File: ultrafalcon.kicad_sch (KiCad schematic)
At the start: 43 parts, among them J1 Conn_01x08_Socket, SW1 RotaryEncoder, SW2 SW_Push, U1 SK6805-EC15, U10 SK6805-EC15, U11 SK6805-EC15, U12 SK6805-EC15, U13 SK6805-EC15, U14 SK6805-EC15, U15 SK6805-EC15, U16 SK6805-EC15, U17 SK6805-EC15, U18 SK6805-EC15, U19 SK6805-EC15, U2 SK6805-EC15, U20 SK6805-EC15, U21 SK6805-EC15, U22 SK6805-EC15, U23 SK6805-EC15, U24 SK6805-EC15, U25 SK6805-EC15, U26 SK6805-EC15, U27 SK6805-EC15, U28 SK6805-EC15, U29 SK6805-EC15, U3 SK6805-EC15, U30 SK6805-EC15, U4 SK6805-EC15, U5 SK6805-EC15, U6 SK6805-EC15, U7 SK6805-EC15, U8 SK6805-EC15, U9 SK6805-EC15

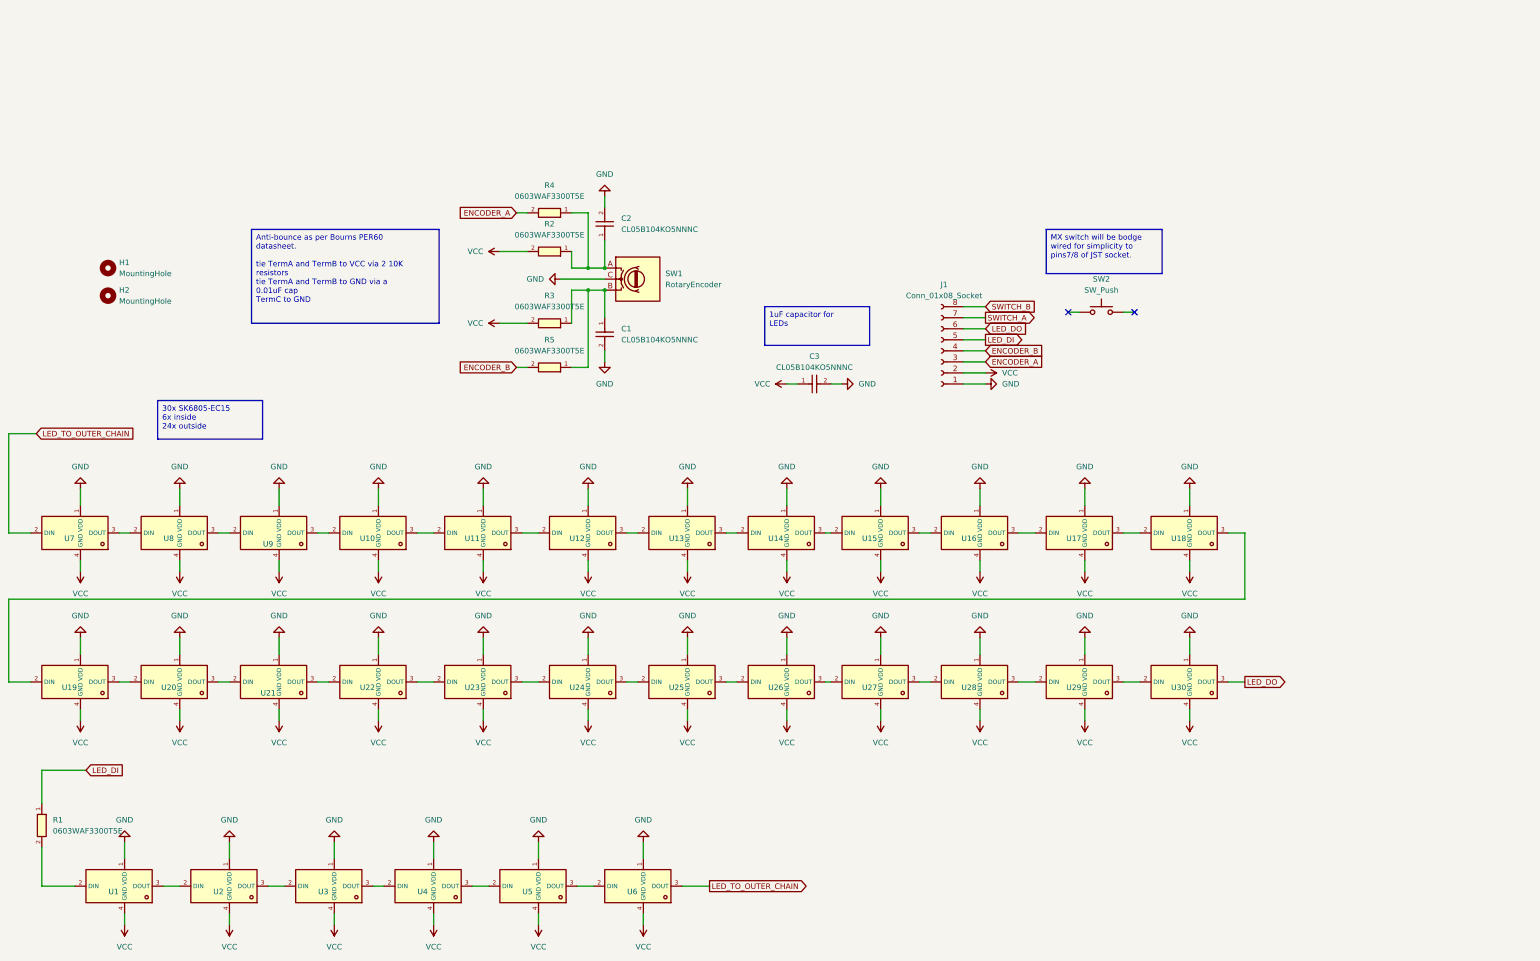
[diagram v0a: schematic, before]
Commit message: replacing the led footprint and symbol, doing the tracing
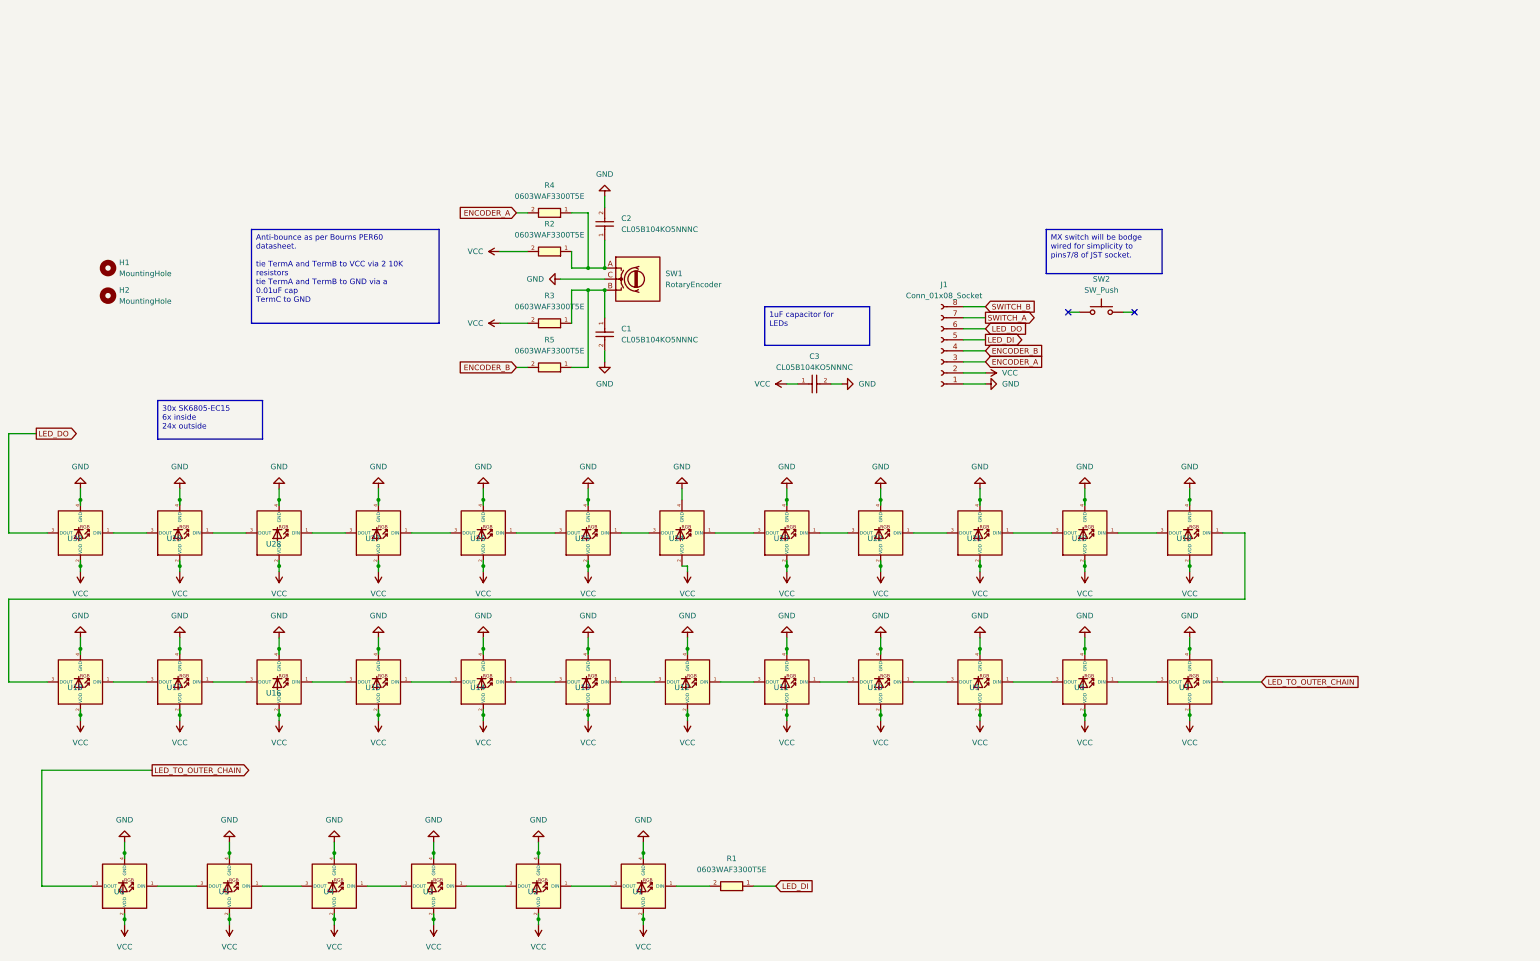
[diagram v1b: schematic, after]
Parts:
- U1: renamed from U6; footprint ct-kicad:LED-SMD_4P-L1.5-W1.5-BL -> ct-kicad:LED_dilemma_SK6805-EC15_1.5x1.5mm_P0.6mm_handsolder; MFN (none) -> Dongguan Opsco Optoelectronics; MPN (none) -> SK6805-EC15; PKG (none) -> SK6805-EC15
- U10: renamed from U27; footprint ct-kicad:LED-SMD_4P-L1.5-W1.5-BL -> ct-kicad:LED_dilemma_SK6805-EC15_1.5x1.5mm_P0.6mm_handsolder; MFN (none) -> Dongguan Opsco Optoelectronics; MPN (none) -> SK6805-EC15; PKG (none) -> SK6805-EC15
- U11: renamed from U26; footprint ct-kicad:LED-SMD_4P-L1.5-W1.5-BL -> ct-kicad:LED_dilemma_SK6805-EC15_1.5x1.5mm_P0.6mm_handsolder; MFN (none) -> Dongguan Opsco Optoelectronics; MPN (none) -> SK6805-EC15; PKG (none) -> SK6805-EC15
- U12: renamed from U25; footprint ct-kicad:LED-SMD_4P-L1.5-W1.5-BL -> ct-kicad:LED_dilemma_SK6805-EC15_1.5x1.5mm_P0.6mm_handsolder; MFN (none) -> Dongguan Opsco Optoelectronics; MPN (none) -> SK6805-EC15; PKG (none) -> SK6805-EC15
- U13: renamed from U24; footprint ct-kicad:LED-SMD_4P-L1.5-W1.5-BL -> ct-kicad:LED_dilemma_SK6805-EC15_1.5x1.5mm_P0.6mm_handsolder; MFN (none) -> Dongguan Opsco Optoelectronics; MPN (none) -> SK6805-EC15; PKG (none) -> SK6805-EC15
- U14: renamed from U23; footprint ct-kicad:LED-SMD_4P-L1.5-W1.5-BL -> ct-kicad:LED_dilemma_SK6805-EC15_1.5x1.5mm_P0.6mm_handsolder; MFN (none) -> Dongguan Opsco Optoelectronics; MPN (none) -> SK6805-EC15; PKG (none) -> SK6805-EC15
- U15: renamed from U22; footprint ct-kicad:LED-SMD_4P-L1.5-W1.5-BL -> ct-kicad:LED_dilemma_SK6805-EC15_1.5x1.5mm_P0.6mm_handsolder; MFN (none) -> Dongguan Opsco Optoelectronics; MPN (none) -> SK6805-EC15; PKG (none) -> SK6805-EC15
- U16: renamed from U21; footprint ct-kicad:LED-SMD_4P-L1.5-W1.5-BL -> ct-kicad:LED_dilemma_SK6805-EC15_1.5x1.5mm_P0.6mm_handsolder; MFN (none) -> Dongguan Opsco Optoelectronics; MPN (none) -> SK6805-EC15; PKG (none) -> SK6805-EC15
- U17: renamed from U20; footprint ct-kicad:LED-SMD_4P-L1.5-W1.5-BL -> ct-kicad:LED_dilemma_SK6805-EC15_1.5x1.5mm_P0.6mm_handsolder; MFN (none) -> Dongguan Opsco Optoelectronics; MPN (none) -> SK6805-EC15; PKG (none) -> SK6805-EC15
- U18: renamed from U19; footprint ct-kicad:LED-SMD_4P-L1.5-W1.5-BL -> ct-kicad:LED_dilemma_SK6805-EC15_1.5x1.5mm_P0.6mm_handsolder; MFN (none) -> Dongguan Opsco Optoelectronics; MPN (none) -> SK6805-EC15; PKG (none) -> SK6805-EC15
- U19: renamed from U18; footprint ct-kicad:LED-SMD_4P-L1.5-W1.5-BL -> ct-kicad:LED_dilemma_SK6805-EC15_1.5x1.5mm_P0.6mm_handsolder; MFN (none) -> Dongguan Opsco Optoelectronics; MPN (none) -> SK6805-EC15; PKG (none) -> SK6805-EC15
- U2: renamed from U5; footprint ct-kicad:LED-SMD_4P-L1.5-W1.5-BL -> ct-kicad:LED_dilemma_SK6805-EC15_1.5x1.5mm_P0.6mm_handsolder; MFN (none) -> Dongguan Opsco Optoelectronics; MPN (none) -> SK6805-EC15; PKG (none) -> SK6805-EC15
- U20: renamed from U17; footprint ct-kicad:LED-SMD_4P-L1.5-W1.5-BL -> ct-kicad:LED_dilemma_SK6805-EC15_1.5x1.5mm_P0.6mm_handsolder; MFN (none) -> Dongguan Opsco Optoelectronics; MPN (none) -> SK6805-EC15; PKG (none) -> SK6805-EC15
- U21: renamed from U16; footprint ct-kicad:LED-SMD_4P-L1.5-W1.5-BL -> ct-kicad:LED_dilemma_SK6805-EC15_1.5x1.5mm_P0.6mm_handsolder; MFN (none) -> Dongguan Opsco Optoelectronics; MPN (none) -> SK6805-EC15; PKG (none) -> SK6805-EC15
- U22: renamed from U15; footprint ct-kicad:LED-SMD_4P-L1.5-W1.5-BL -> ct-kicad:LED_dilemma_SK6805-EC15_1.5x1.5mm_P0.6mm_handsolder; MFN (none) -> Dongguan Opsco Optoelectronics; MPN (none) -> SK6805-EC15; PKG (none) -> SK6805-EC15
- U23: renamed from U14; footprint ct-kicad:LED-SMD_4P-L1.5-W1.5-BL -> ct-kicad:LED_dilemma_SK6805-EC15_1.5x1.5mm_P0.6mm_handsolder; MFN (none) -> Dongguan Opsco Optoelectronics; MPN (none) -> SK6805-EC15; PKG (none) -> SK6805-EC15
- U24: renamed from U13; footprint ct-kicad:LED-SMD_4P-L1.5-W1.5-BL -> ct-kicad:LED_dilemma_SK6805-EC15_1.5x1.5mm_P0.6mm_handsolder; MFN (none) -> Dongguan Opsco Optoelectronics; MPN (none) -> SK6805-EC15; PKG (none) -> SK6805-EC15
- U25: renamed from U12; footprint ct-kicad:LED-SMD_4P-L1.5-W1.5-BL -> ct-kicad:LED_dilemma_SK6805-EC15_1.5x1.5mm_P0.6mm_handsolder; MFN (none) -> Dongguan Opsco Optoelectronics; MPN (none) -> SK6805-EC15; PKG (none) -> SK6805-EC15
- U26: renamed from U11; footprint ct-kicad:LED-SMD_4P-L1.5-W1.5-BL -> ct-kicad:LED_dilemma_SK6805-EC15_1.5x1.5mm_P0.6mm_handsolder; MFN (none) -> Dongguan Opsco Optoelectronics; MPN (none) -> SK6805-EC15; PKG (none) -> SK6805-EC15
- U27: renamed from U10; footprint ct-kicad:LED-SMD_4P-L1.5-W1.5-BL -> ct-kicad:LED_dilemma_SK6805-EC15_1.5x1.5mm_P0.6mm_handsolder; MFN (none) -> Dongguan Opsco Optoelectronics; MPN (none) -> SK6805-EC15; PKG (none) -> SK6805-EC15
- U28: renamed from U9; footprint ct-kicad:LED-SMD_4P-L1.5-W1.5-BL -> ct-kicad:LED_dilemma_SK6805-EC15_1.5x1.5mm_P0.6mm_handsolder; MFN (none) -> Dongguan Opsco Optoelectronics; MPN (none) -> SK6805-EC15; PKG (none) -> SK6805-EC15
- U29: renamed from U8; footprint ct-kicad:LED-SMD_4P-L1.5-W1.5-BL -> ct-kicad:LED_dilemma_SK6805-EC15_1.5x1.5mm_P0.6mm_handsolder; MFN (none) -> Dongguan Opsco Optoelectronics; MPN (none) -> SK6805-EC15; PKG (none) -> SK6805-EC15
- U3: renamed from U4; footprint ct-kicad:LED-SMD_4P-L1.5-W1.5-BL -> ct-kicad:LED_dilemma_SK6805-EC15_1.5x1.5mm_P0.6mm_handsolder; MFN (none) -> Dongguan Opsco Optoelectronics; MPN (none) -> SK6805-EC15; PKG (none) -> SK6805-EC15
- U30: renamed from U7; footprint ct-kicad:LED-SMD_4P-L1.5-W1.5-BL -> ct-kicad:LED_dilemma_SK6805-EC15_1.5x1.5mm_P0.6mm_handsolder; MFN (none) -> Dongguan Opsco Optoelectronics; MPN (none) -> SK6805-EC15; PKG (none) -> SK6805-EC15
- U4: renamed from U3; footprint ct-kicad:LED-SMD_4P-L1.5-W1.5-BL -> ct-kicad:LED_dilemma_SK6805-EC15_1.5x1.5mm_P0.6mm_handsolder; MFN (none) -> Dongguan Opsco Optoelectronics; MPN (none) -> SK6805-EC15; PKG (none) -> SK6805-EC15
- U5: renamed from U2; footprint ct-kicad:LED-SMD_4P-L1.5-W1.5-BL -> ct-kicad:LED_dilemma_SK6805-EC15_1.5x1.5mm_P0.6mm_handsolder; MFN (none) -> Dongguan Opsco Optoelectronics; MPN (none) -> SK6805-EC15; PKG (none) -> SK6805-EC15
- U6: renamed from U1; footprint ct-kicad:LED-SMD_4P-L1.5-W1.5-BL -> ct-kicad:LED_dilemma_SK6805-EC15_1.5x1.5mm_P0.6mm_handsolder; MFN (none) -> Dongguan Opsco Optoelectronics; MPN (none) -> SK6805-EC15; PKG (none) -> SK6805-EC15
- U7: renamed from U30; footprint ct-kicad:LED-SMD_4P-L1.5-W1.5-BL -> ct-kicad:LED_dilemma_SK6805-EC15_1.5x1.5mm_P0.6mm_handsolder; MFN (none) -> Dongguan Opsco Optoelectronics; MPN (none) -> SK6805-EC15; PKG (none) -> SK6805-EC15
- U8: renamed from U29; footprint ct-kicad:LED-SMD_4P-L1.5-W1.5-BL -> ct-kicad:LED_dilemma_SK6805-EC15_1.5x1.5mm_P0.6mm_handsolder; MFN (none) -> Dongguan Opsco Optoelectronics; MPN (none) -> SK6805-EC15; PKG (none) -> SK6805-EC15
- U9: renamed from U28; footprint ct-kicad:LED-SMD_4P-L1.5-W1.5-BL -> ct-kicad:LED_dilemma_SK6805-EC15_1.5x1.5mm_P0.6mm_handsolder; MFN (none) -> Dongguan Opsco Optoelectronics; MPN (none) -> SK6805-EC15; PKG (none) -> SK6805-EC15
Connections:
- net GND: now also U1.4 (GND), U10.4 (GND), U11.4 (GND), U12.4 (GND), U13.4 (GND), U14.4 (GND), U15.4 (GND), U16.4 (GND), U17.4 (GND), U18.4 (GND), U19.4 (GND), U2.4 (GND), U20.4 (GND), U21.4 (GND), U22.4 (GND), U23.4 (GND), U24.4 (GND), U25.4 (GND), U26.4 (GND), U27.4 (GND), U28.4 (GND), U29.4 (GND), U3.4 (GND), U30.4 (GND), U4.4 (GND), U5.4 (GND), U6.4 (GND), U7.4 (GND), U8.4 (GND), U9.4 (GND); no longer U1.1 (VDD), U10.1 (VDD), U11.1 (VDD), U12.1 (VDD), U13.1 (VDD), U14.1 (VDD), U15.1 (VDD), U16.1 (VDD), U17.1 (VDD), U18.1 (VDD), U19.1 (VDD), U2.1 (VDD), U20.1 (VDD), U21.1 (VDD), U22.1 (VDD), U23.1 (VDD), U24.1 (VDD), U25.1 (VDD), U26.1 (VDD), U27.1 (VDD), U28.1 (VDD), U29.1 (VDD), U3.1 (VDD), U30.1 (VDD), U4.1 (VDD), U5.1 (VDD), U6.1 (VDD), U7.1 (VDD), U8.1 (VDD), U9.1 (VDD)
- net LED_DO: now also U30.3 (DOUT); no longer U7.3 (DOUT)
- net LED_TO_OUTER_CHAIN: now also U6.3 (DOUT), U7.1 (DIN); no longer U1.3 (DOUT), U30.2 (DIN)
- net VCC: now also U1.2 (VDD), U10.2 (VDD), U11.2 (VDD), U12.2 (VDD), U13.2 (VDD), U14.2 (VDD), U15.2 (VDD), U16.2 (VDD), U17.2 (VDD), U18.2 (VDD), U19.2 (VDD), U2.2 (VDD), U20.2 (VDD), U21.2 (VDD), U22.2 (VDD), U23.2 (VDD), U24.2 (VDD), U25.2 (VDD), U26.2 (VDD), U27.2 (VDD), U28.2 (VDD), U29.2 (VDD), U3.2 (VDD), U30.2 (VDD), U4.2 (VDD), U5.2 (VDD), U6.2 (VDD), U7.2 (VDD), U8.2 (VDD), U9.2 (VDD); no longer U1.4 (GND), U10.4 (GND), U11.4 (GND), U12.4 (GND), U13.4 (GND), U14.4 (GND), U15.4 (GND), U16.4 (GND), U17.4 (GND), U18.4 (GND), U19.4 (GND), U2.4 (GND), U20.4 (GND), U21.4 (GND), U22.4 (GND), U23.4 (GND), U24.4 (GND), U25.4 (GND), U26.4 (GND), U27.4 (GND), U28.4 (GND), U29.4 (GND), U3.4 (GND), U30.4 (GND), U4.4 (GND), U5.4 (GND), U6.4 (GND), U7.4 (GND), U8.4 (GND), U9.4 (GND)
- net at U20.3 (DOUT): now also U21.1 (DIN); no longer U19.2 (DIN)
- net at U19.3 (DOUT): now also U20.1 (DIN); no longer U18.2 (DIN)
- net at U27.3 (DOUT): now also U28.1 (DIN); no longer U26.2 (DIN)
- net at U26.3 (DOUT): now also U27.1 (DIN); no longer U25.2 (DIN)
- net at U5.3 (DOUT): now also U6.1 (DIN); no longer U4.2 (DIN)
- net at U4.3 (DOUT): now also U5.1 (DIN); no longer U3.2 (DIN)
- net at R1.2: now also U1.1 (DIN); no longer U6.2 (DIN)
- net at U11.3 (DOUT): now also U12.1 (DIN); no longer U10.2 (DIN)
- net at U10.3 (DOUT): now also U11.1 (DIN); no longer U9.2 (DIN)
- net at U22.3 (DOUT): now also U23.1 (DIN); no longer U21.2 (DIN)
- net at U21.3 (DOUT): now also U22.1 (DIN); no longer U20.2 (DIN)
- net at U12.3 (DOUT): now also U13.1 (DIN); no longer U11.2 (DIN)
- net at U3.3 (DOUT): now also U4.1 (DIN); no longer U2.2 (DIN)
- net at U2.3 (DOUT): now also U3.1 (DIN); no longer U1.2 (DIN)
- net at U23.3 (DOUT): now also U24.1 (DIN); no longer U22.2 (DIN)
- net at U29.3 (DOUT): now also U30.1 (DIN); no longer U28.2 (DIN)
- net at U28.3 (DOUT): now also U29.1 (DIN); no longer U27.2 (DIN)
- net at U14.3 (DOUT): now also U15.1 (DIN); no longer U13.2 (DIN)
- net at U13.3 (DOUT): now also U14.1 (DIN); no longer U12.2 (DIN)
- net at U18.3 (DOUT): now also U19.1 (DIN); no longer U17.2 (DIN)
- net at U25.3 (DOUT): now also U26.1 (DIN); no longer U24.2 (DIN)
- net at U8.3 (DOUT): now also U9.1 (DIN); no longer U7.2 (DIN)
- net at U15.3 (DOUT): now also U16.1 (DIN); no longer U14.2 (DIN)
- net at U16.3 (DOUT): now also U17.1 (DIN); no longer U15.2 (DIN)
- net at U24.3 (DOUT): now also U25.1 (DIN); no longer U23.2 (DIN)
- net at U9.3 (DOUT): now also U10.1 (DIN); no longer U8.2 (DIN)
- net at U17.3 (DOUT): now also U18.1 (DIN); no longer U16.2 (DIN)
- new net: U1.3 (DOUT), U2.1 (DIN)
- new net: U7.3 (DOUT), U8.1 (DIN)

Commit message: moving text around, adding rear labels, updating footprints
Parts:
- added LOGO1: **REF, ct-kicad:awesome-logo, symbol ct-kicad:awesome-logo
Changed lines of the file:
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@@
+    )
+  )
+  (symbol (lib_id "ct-kicad:awesome-logo") (at 41.91 96.52 0) (unit 1)
+    (in_bom no) (on_board yes) (dnp no) (fields_autoplaced)
+    (property "Reference" "LOGO1" (at 44.45 95.25 0)
+      (effects (font (size 1.27 1.27)) (justify left))
+    )
+    (property "Value" "**REF" (at 44.45 97.79 0)
+      (effects (font (size 1.27 1.27)) (justify left))
+    )
+    (property "Footprint" "ct-kicad:awesome-logo" (at 41.91 96.52 0)
+      (effects (font (size 1.27 1.27)) hide)
+    )
+    (property "Datasheet" "" (at 41.91 96.52 0)
+      (effects (font (size 1.27 1.27)) hide)
+    )
+    (instances
+      (project "ultrafalcon"
+        (path "/7e990e0f-d17d-4d94-84c9-ab822ccf2d6e"
+          (reference "LOGO1") (unit 1)
+        )
+      )
     )
   )

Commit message: getting the board ready for pcbway
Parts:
- C1, C2: value CL05B104KO5NNNC -> 0.01uF
- C3: value CL05B104KO5NNNC -> 100uF
- H1, H2, J1, SW2: now left out of the parts list
- R1: value 0603WAF3300T5E -> 330
- R2, R3, R4, R5: value 0603WAF3300T5E -> 10k
- SW1: value RotaryEncoder -> PER601-P117-N0015
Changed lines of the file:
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@@
       (effects (font (size 1.27 1.27)) (justify left))
     )
-    (property "Value" "RotaryEncoder" (at 170.18 86.36 0)
+    (property "Value" "PER601-P117-N0015" (at 170.18 86.36 0)
       (effects (font (size 1.27 1.27)) (justify left))
     )
@@
   )
   (symbol (lib_id "Mechanical:MountingHole") (at 41.91 88.9 0) (unit 1)
-    (in_bom yes) (on_board yes) (dnp no) (fields_autoplaced)
+    (in_bom no) (on_board yes) (dnp no) (fields_autoplaced)
     (property "Reference" "H2" (at 44.45 87.63 0)
       (effects (font (size 1.27 1.27)) (justify left))
@@
       (effects (font (size 1.27 1.27)))
     )
-    (property "Value" "0603WAF3300T5E" (at 143.51 74.93 0)
+    (property "Value" "10k" (at 143.51 74.93 0)
       (effects (font (size 1.27 1.27)))
     )
@@
   )
   (symbol (lib_id "Switch:SW_Push") (at 270.51 92.71 0) (unit 1)
-    (in_bom yes) (on_board yes) (dnp no) (fields_autoplaced)
+    (in_bom no) (on_board yes) (dnp no) (fields_autoplaced)
     (property "Reference" "SW2" (at 270.51 85.09 0)
       (effects (font (size 1.27 1.27)))
@@
       (effects (font (size 1.27 1.27)))
     )
-    (property "Value" "0603WAF3300T5E" (at 143.51 91.44 0)
+    (property "Value" "10k" (at 143.51 91.44 0)
       (effects (font (size 1.27 1.27)))
     )
@@
       (effects (font (size 1.27 1.27)))
     )
-    (property "Value" "CL05B104KO5NNNC" (at 204.47 105.41 0)
+    (property "Value" "100uF" (at 204.47 105.41 0)
       (effects (font (size 1.27 1.27)))
     )
@@
       (effects (font (size 1.27 1.27)))
     )
-    (property "Value" "0603WAF3300T5E" (at 185.42 220.98 0)
+    (property "Value" "330" (at 185.42 220.98 0)
       (effects (font (size 1.27 1.27)))
     )
@@
       (effects (font (size 1.27 1.27)) (justify left))
     )
-    (property "Value" "CL05B104KO5NNNC" (at 160.02 99.06 90)
+    (property "Value" "0.01uF" (at 160.02 99.06 90)
       (effects (font (size 1.27 1.27)) (justify left))
     )
@@
       (effects (font (size 1.27 1.27)) (justify right))
     )
-    (property "Value" "CL05B104KO5NNNC" (at 160.02 73.66 90)
+    (property "Value" "0.01uF" (at 160.02 73.66 90)
       (effects (font (size 1.27 1.27)) (justify right))
     )
@@
       (effects (font (size 1.27 1.27)))
     )
-    (property "Value" "0603WAF3300T5E" (at 143.51 101.6 0)
+    (property "Value" "10k" (at 143.51 101.6 0)
       (effects (font (size 1.27 1.27)))
     )
@@
   )
   (symbol (lib_id "Connector:Conn_01x08_Socket") (at 233.68 101.6 180) (unit 1)
-    (in_bom yes) (on_board yes) (dnp no) (fields_autoplaced)
+    (in_bom no) (on_board yes) (dnp no) (fields_autoplaced)
     (property "Reference" "J1" (at 234.315 86.36 0)
       (effects (font (size 1.27 1.27)))
@@
       (effects (font (size 1.27 1.27)))
     )
-    (property "Value" "0603WAF3300T5E" (at 143.51 66.04 0)
+    (property "Value" "10k" (at 143.51 66.04 0)
       (effects (font (size 1.27 1.27)))
     )
@@
   )
   (symbol (lib_id "Mechanical:MountingHole") (at 41.91 82.55 0) (unit 1)
-    (in_bom yes) (on_board yes) (dnp no) (fields_autoplaced)
+    (in_bom no) (on_board yes) (dnp no) (fields_autoplaced)
     (property "Reference" "H1" (at 44.45 81.28 0)
       (effects (font (size 1.27 1.27)) (justify left))
